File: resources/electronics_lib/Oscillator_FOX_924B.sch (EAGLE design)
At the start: 1 part

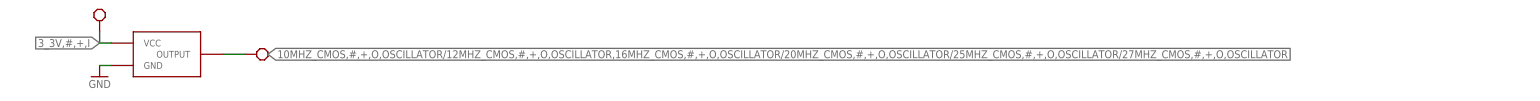
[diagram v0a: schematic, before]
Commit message: Fixed typo in Oscillator block.
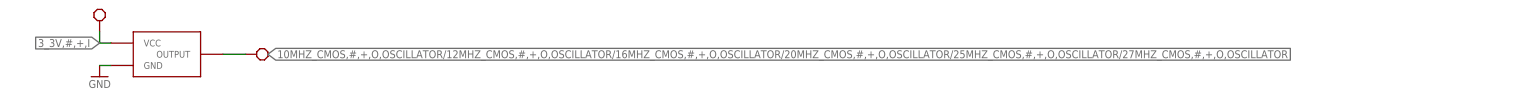
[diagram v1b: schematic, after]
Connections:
- net 10MHZ_CMOS,#,+,O,OSCILLATOR/12MHZ_CMOS,#,+,O,OSCILLATOR,16MHZ_CMOS,#,+,O,OSCILLATOR/20MHZ_CMOS,#,+,O,OSCILLATOR/25MHZ_CMOS,#,+,O,OSCILLATOR/27MHZ_CMOS,#,+,O,OSCILLATOR renamed 10MHZ_CMOS,#,+,O,OSCILLATOR/12MHZ_CMOS,#,+,O,OSCILLATOR/16MHZ_CMOS,#,+,O,OSCILLATOR/20MHZ_CMOS,#,+,O,OSCILLATOR/25MHZ_CMOS,#,+,O,OSCILLATOR/27MHZ_CMOS,#,+,O,OSCILLATOR
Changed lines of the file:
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@@
 </segment>
 </net>
-<net name="10MHZ_CMOS,#,+,O,OSCILLATOR/12MHZ_CMOS,#,+,O,OSCILLATOR,16MHZ_CMOS,#,+,O,OSCILLATOR/20MHZ_CMOS,#,+,O,OSCILLATOR/25MHZ_CMOS,#,+,O,OSCILLATOR/27MHZ_CMOS,#,+,O,OSCILLATOR" class="0">
+<net name="10MHZ_CMOS,#,+,O,OSCILLATOR/12MHZ_CMOS,#,+,O,OSCILLATOR/16MHZ_CMOS,#,+,O,OSCILLATOR/20MHZ_CMOS,#,+,O,OSCILLATOR/25MHZ_CMOS,#,+,O,OSCILLATOR/27MHZ_CMOS,#,+,O,OSCILLATOR" class="0">
 <segment>
 <pinref part="OSC1" gate="G$1" pin="OUTPUT"/>
